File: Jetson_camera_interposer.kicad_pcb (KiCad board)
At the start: 6 copper layers, 82.1 x 75 mm, 19 parts, among them J1 QSH-060-01-L-D-A, J2 QTH-060-01-L-D-A, J21 Conn_01x01, J22 Conn_01x01, J23 Conn_01x01, J24 Conn_01x01, J25 Conn_01x01, J26 Conn_01x01, J3 Conn_01x01, J4 Conn_01x01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

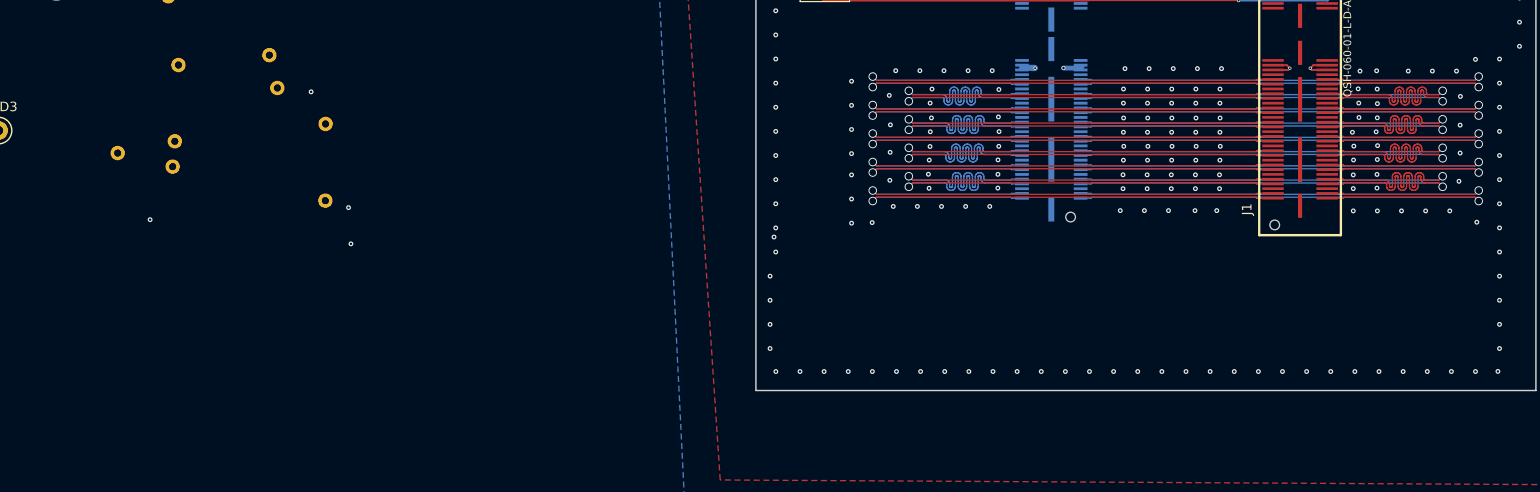
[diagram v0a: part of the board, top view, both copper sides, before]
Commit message: removed vias
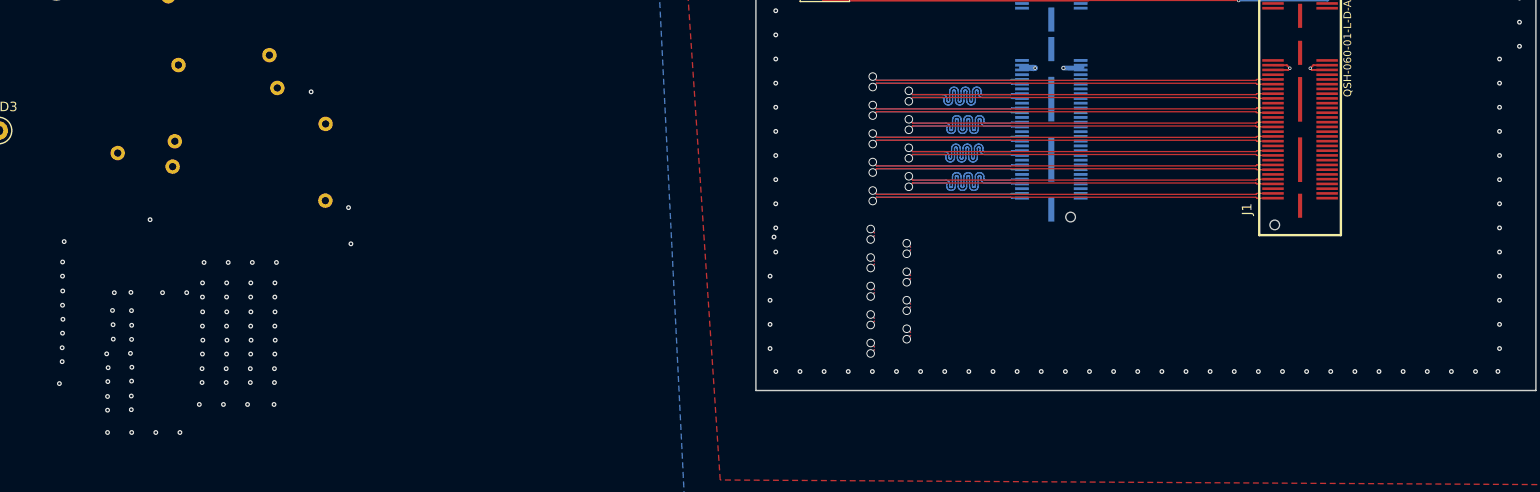
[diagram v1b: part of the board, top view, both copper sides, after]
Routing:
- net /CSI0_D1_N: track 58.3 -> 1.13 mm
- net /CSI2_CLK_P: track 58.3 -> 1.13 mm
- net /CSI4_D0_P: track 58.3 -> 1.13 mm
- net /CSI4_D0_N: track 58.3 -> 1.13 mm
- net /CSI2_CLK_N: track 58.3 -> 1.13 mm
- net /CSI0_D0_P: track 58.3 -> 1.13 mm
- net /CSI0_D0_N: track 58.3 -> 1.13 mm
- net /CSI0_D1_P: track 58.3 -> 1.13 mm
- net /CSI4_D1_N: track 58.3 -> 1.13 mm
- net /CSI4_D1_P: track 58.3 -> 1.13 mm
- net /CSI4_CLK_P: track 58.3 -> 1.13 mm
- net /CSI2_D0_P: track 58.3 -> 1.13 mm
- net /CSI2_D1_P: track 58.3 -> 1.13 mm
- net /CSI0_CLK_P: track 58.3 -> 1.13 mm
- net /CSI4_CLK_N: track 58.3 -> 1.13 mm
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
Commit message: DRC OK
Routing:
- net /CSI0_D1_N: track 1.13 -> 58.3 mm
- net /CSI2_CLK_P: track 1.13 -> 58.3 mm
- net /CSI4_D0_P: track 1.13 -> 58.3 mm
- net /CSI4_D0_N: track 1.13 -> 58.3 mm
- net /CSI2_CLK_N: track 1.13 -> 58.3 mm
- net /CSI0_D0_P: track 1.13 -> 58.3 mm
- net /CSI0_D0_N: track 1.13 -> 58.3 mm
- net /CSI0_D1_P: track 1.13 -> 58.3 mm
- net /CSI4_D1_N: track 1.13 -> 58.3 mm
- net /CSI4_D1_P: track 1.13 -> 58.3 mm
- net /CSI4_CLK_P: track 1.13 -> 58.3 mm
- net /CSI2_D0_P: track 1.13 -> 58.3 mm
- net /CSI2_D1_P: track 1.13 -> 58.3 mm
- net /CSI0_CLK_P: track 1.13 -> 58.3 mm
- net /CSI2_D0_N: track 1.13 -> 58.3 mm
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
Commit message: Done routing
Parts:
- removed GND1, GND2, GND3: TestP, TX2_Footprints:test_point
- removed J21, J22, J23, J24, J25, J4, J5, J6: Conn_01x01, TX2_Footprints:ground_probe
- added J7: Conn_01x01, Pin_Headers:Pin_Header_Straight_1x01_Pitch2.54mm, F.Cu at (4.15, 39.9)
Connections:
- J1 pad 117: (no net) -> /CAM_INTR
- J1 pad 119: (no net) -> /VSYS_EN
- J2 pad 117: (no net) -> /CAM_INTR
- J2 pad 119: (no net) -> /VSYS_EN
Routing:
- net /VSYS_EN: track 0.00 -> 27.4 mm, vias 0 -> 1
- net /CAM_INTR: track 0.00 -> 26.8 mm, vias 0 -> 2
- net /I2C_GP0_DAT_1V8_J: track 62.4 -> 66.1 mm
- net /VDD_SYS: track 32.3 -> 33.3 mm

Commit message: placed jumpers
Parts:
- removed GND4, I2C_CLK2, I2C_DAT2: TestP, TX2_Footprints:test_point
- removed J26: Conn_01x01, TX2_Footprints:ground_probe
- added J10: JETSON_1V8, Pin_Headers:Pin_Header_Straight_1x01_Pitch2.54mm, F.Cu at (112.2, 76.8)
- added J11: VDD_3V3, Pin_Headers:Pin_Header_Straight_1x01_Pitch2.54mm, F.Cu at (108.4, 84.1)
- added J12: VDD_SYS, Pin_Headers:Pin_Header_Straight_1x01_Pitch2.54mm, F.Cu at (123.3, 71.3)
- added J13: VDD_CAM_FQ_HV_CAM, Pin_Headers:Pin_Header_Straight_1x01_Pitch2.54mm, F.Cu at (130.5, 103.1)
- added J14: CAM_AF_PWDN, Pin_Headers:Pin_Header_Straight_1x01_Pitch2.54mm, F.Cu at (164.2, 101.6)
- added J15: CAM_FLASH_EN, Pin_Headers:Pin_Header_Straight_1x01_Pitch2.54mm, F.Cu at (164.2, 94.4)
- added J16: JETSON_1V2, Pin_Headers:Pin_Header_Straight_1x01_Pitch2.54mm, F.Cu at (164.2, 98.0)
- added J17: VDD_IR, Pin_Headers:Pin_Header_Straight_1x01_Pitch2.54mm, F.Cu at (160.6, 90.8)
- added J18: IR_READY, Pin_Headers:Pin_Header_Straight_1x01_Pitch2.54mm, F.Cu at (164.2, 90.8)
- added J19: CAM_INTR, Pin_Headers:Pin_Header_Straight_1x01_Pitch2.54mm, F.Cu at (164.2, 83.5)
- added J20: IR_TRIGGER, Pin_Headers:Pin_Header_Straight_1x01_Pitch2.54mm, F.Cu at (164.2, 87.2)
- added J21: VSYS_EN, Pin_Headers:Pin_Header_Straight_1x01_Pitch2.54mm, F.Cu at (164.2, 79.9)
- added J22: GND, Pin_Headers:Pin_Header_Straight_1x01_Pitch2.54mm, F.Cu at (163.0, 127.2)
- added J23: GND, Pin_Headers:Pin_Header_Straight_1x01_Pitch2.54mm, F.Cu at (96.6, 132.5)
- added J4: DVDD_CAM_LV, Pin_Headers:Pin_Header_Straight_1x01_Pitch2.54mm, F.Cu at (111.6, 104.0)
- added J5: AVDD_CAM, Pin_Headers:Pin_Header_Straight_1x01_Pitch2.54mm, F.Cu at (95.4, 104.0)
- added J6: VDD_AF, Pin_Headers:Pin_Header_Straight_1x01_Pitch2.54mm, F.Cu at (99.0, 104.0)
- added J9: CAM_VSYNC, Pin_Headers:Pin_Header_Straight_1x01_Pitch2.54mm, F.Cu at (126.9, 103.1)
- J3: value Conn_01x01 -> GND; footprint TX2_Footprints:ground_probe -> Pin_Headers:Pin_Header_Straight_1x01_Pitch2.54mm
- J7: value Conn_01x01 -> GND
- moved J7 114.9 mm to (94.0, 111.5)
- moved J3 95.4 mm to (110.7, 70.8)
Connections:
- J7 pad 1: (no net) -> Earth
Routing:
- net /CAM0_RST: track 33.6 -> 34.8 mm
- net /CAM1_RST_L_J: track 61.8 -> 62.8 mm
- net /DVDD_CAM_LV: track 47.8 -> 46.8 mm
- net /CAM0_MCLK_J: track 61.3 -> 62.1 mm

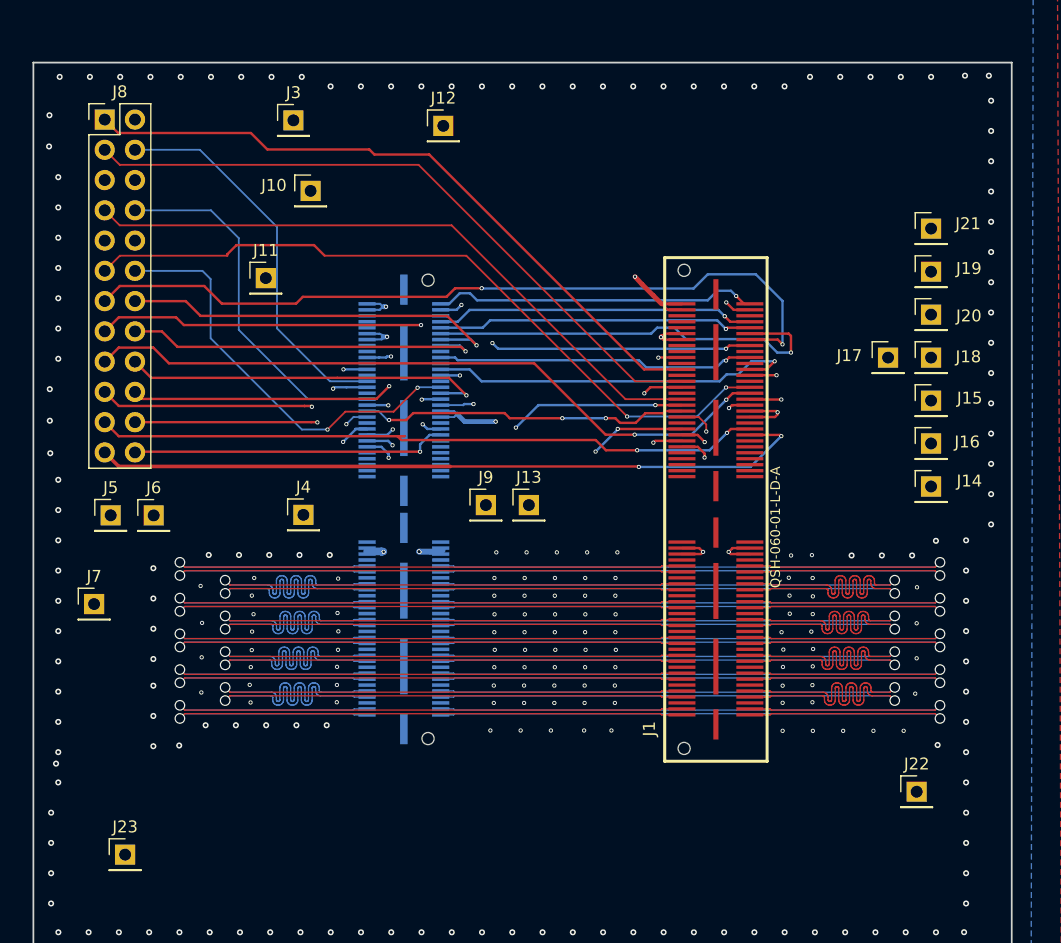
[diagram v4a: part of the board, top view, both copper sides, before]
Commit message: placed debug connectors
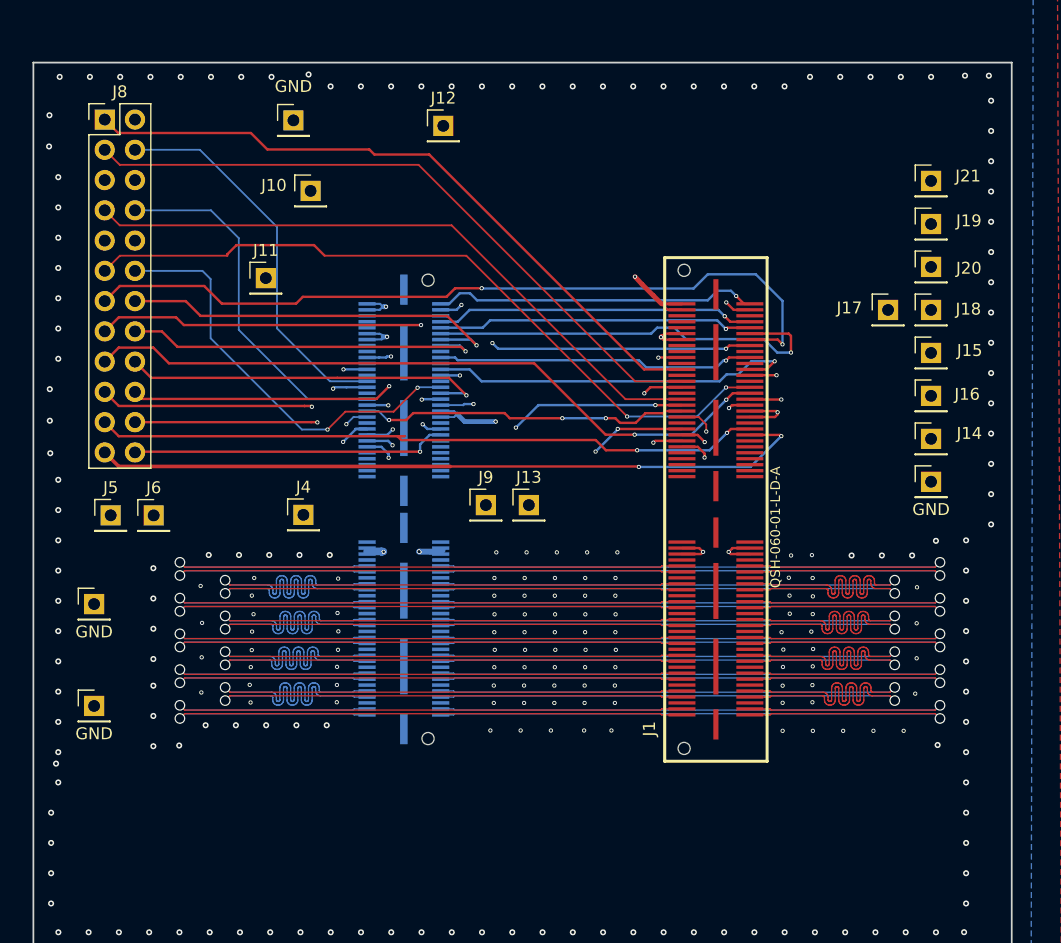
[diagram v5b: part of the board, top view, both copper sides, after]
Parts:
- moved J22 26.0 mm to (164.2, 101.2)
- moved J23 12.7 mm to (94.0, 120.0)
- moved J14 4.00 mm to (164.2, 97.6)
- moved J15 4.00 mm to (164.2, 90.4)
- moved J16 4.00 mm to (164.2, 94.0)
- moved J17 4.00 mm to (160.6, 86.8)
- moved J18 4.00 mm to (164.2, 86.8)
- moved J19 4.00 mm to (164.2, 79.5)
- moved J20 4.00 mm to (164.2, 83.2)
- moved J21 4.00 mm to (164.2, 75.9)
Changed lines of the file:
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@@
   )
   (module Pin_Headers:Pin_Header_Straight_1x01_Pitch2.54mm (layer F.Cu)
-    (at 164.25 101.58)
+    (at 164.25 97.58)
     (descr "Through hole straight pin header, 1x01, 2.54mm pitch, single row")
     (tags "Through hole pin header THT 1x01 2.54mm single row")
@@
   )
   (module Pin_Headers:Pin_Header_Straight_1x01_Pitch2.54mm (layer F.Cu)
-    (at 164.25 94.37)
+    (at 164.25 90.37)
     (descr "Through hole straight pin header, 1x01, 2.54mm pitch, single row")
     (tags "Through hole pin header THT 1x01 2.54mm single row")
@@
   )
   (module Pin_Headers:Pin_Header_Straight_1x01_Pitch2.54mm (layer F.Cu)
-    (at 164.25 97.97)
+    (at 164.25 93.97)
     (descr "Through hole straight pin header, 1x01, 2.54mm pitch, single row")
     (tags "Through hole pin header THT 1x01 2.54mm single row")
@@
   )
   (module Pin_Headers:Pin_Header_Straight_1x01_Pitch2.54mm (layer F.Cu)
-    (at 160.64 90.76)
+    (at 160.64 86.76)
     (descr "Through hole straight pin header, 1x01, 2.54mm pitch, single row")
     (tags "Through hole pin header THT 1x01 2.54mm single row")
@@
   )
   (module Pin_Headers:Pin_Header_Straight_1x01_Pitch2.54mm (layer F.Cu)
-    (at 164.25 90.76)
+    (at 164.25 86.76)
     (descr "Through hole straight pin header, 1x01, 2.54mm pitch, single row")
     (tags "Through hole pin header THT 1x01 2.54mm single row")
@@
   )
   (module Pin_Headers:Pin_Header_Straight_1x01_Pitch2.54mm (layer F.Cu)
-    (at 164.25 83.55)
+    (at 164.25 79.55)
     (descr "Through hole straight pin header, 1x01, 2.54mm pitch, single row")
     (tags "Through hole pin header THT 1x01 2.54mm single row")
@@
   )
   (module Pin_Headers:Pin_Header_Straight_1x01_Pitch2.54mm (layer F.Cu)
-    (at 164.25 87.15)
+    (at 164.25 83.15)
     (descr "Through hole straight pin header, 1x01, 2.54mm pitch, single row")
     (tags "Through hole pin header THT 1x01 2.54mm single row")
@@
   )
   (module Pin_Headers:Pin_Header_Straight_1x01_Pitch2.54mm (layer F.Cu)
-    (at 164.25 79.93)
+    (at 164.25 75.93)
     (descr "Through hole straight pin header, 1x01, 2.54mm pitch, single row")
     (tags "Through hole pin header THT 1x01 2.54mm single row")
@@
     (descr "Through hole straight pin header, 1x01, 2.54mm pitch, single row")
     (tags "Through hole pin header THT 1x01 2.54mm single row")
-    (fp_text reference J3 (at 0 -2.33) (layer F.SilkS)
-      (effects (font (size 1 1) (thickness 0.15)))
-    )
-    (fp_text value GND (at 0 2.33) (layer F.Fab)
+    (fp_text reference J3 (at 0 -2.33) (layer F.SilkS) hide
+      (effects (font (size 1 1) (thickness 0.15)))
+    )
+    (fp_text value GND (at 0 -2.85) (layer F.SilkS)
       (effects (font (size 1 1) (thickness 0.15)))
     )
@@
     (descr "Through hole straight pin header, 1x01, 2.54mm pitch, single row")
     (tags "Through hole pin header THT 1x01 2.54mm single row")
-    (fp_text reference J7 (at 0 -2.33) (layer F.SilkS)
-      (effects (font (size 1 1) (thickness 0.15)))
-    )
-    (fp_text value GND (at 0 2.33) (layer F.Fab)
+    (fp_text reference J7 (at 0 -2.33) (layer F.SilkS) hide
+      (effects (font (size 1 1) (thickness 0.15)))
+    )
+    (fp_text value GND (at 0 2.33) (layer F.SilkS)
       (effects (font (size 1 1) (thickness 0.15)))
     )
@@
   )
   (module Pin_Headers:Pin_Header_Straight_1x01_Pitch2.54mm (layer F.Cu)
-    (at 163.04 127.2)
-    (descr "Through hole straight pin header, 1x01, 2.54mm pitch, single row")
-    (tags "Through hole pin header THT 1x01 2.54mm single row")
-    (fp_text reference J22 (at 0 -2.33) (layer F.SilkS)
-      (effects (font (size 1 1) (thickness 0.15)))
-    )
-    (fp_text value GND (at 0 2.33) (layer F.Fab)
+    (at 164.25 101.18)
+    (descr "Through hole straight pin header, 1x01, 2.54mm pitch, single row")
+    (tags "Through hole pin header THT 1x01 2.54mm single row")
+    (fp_text reference J22 (at 0 -2.33) (layer F.SilkS) hide
+      (effects (font (size 1 1) (thickness 0.15)))
+    )
+    (fp_text value GND (at 0 2.33) (layer F.SilkS)
       (effects (font (size 1 1) (thickness 0.15)))
     )
@@
   )
   (module Pin_Headers:Pin_Header_Straight_1x01_Pitch2.54mm (layer F.Cu)
-    (at 96.6 132.48)
-    (descr "Through hole straight pin header, 1x01, 2.54mm pitch, single row")
-    (tags "Through hole pin header THT 1x01 2.54mm single row")
-    (fp_text reference J23 (at 0 -2.33) (layer F.SilkS)
-      (effects (font (size 1 1) (thickness 0.15)))
-    )
-    (fp_text value GND (at 0 2.33) (layer F.Fab)
+    (at 94 120)
+    (descr "Through hole straight pin header, 1x01, 2.54mm pitch, single row")
+    (tags "Through hole pin header THT 1x01 2.54mm single row")
+    (fp_text reference J23 (at 0 -2.33) (layer F.SilkS) hide
+      (effects (font (size 1 1) (thickness 0.15)))
+    )
+    (fp_text value GND (at 0 2.33) (layer F.SilkS)
       (effects (font (size 1 1) (thickness 0.15)))
     )
@@
   )
   (dimension 10.040603 (width 0.15) (layer Dwgs.User)
-    (gr_text "10.041 mm" (at 155.836812 125.660505 359.3722825) (layer Dwgs.User)
-      (effects (font (size 1 1) (thickness 0.15)))
-    )
-    (feature1 (pts (xy 160.84 127.25) (xy 160.848995 126.429042)))
-    (feature2 (pts (xy 150.8 127.14) (xy 150.808995 126.319042)))
-    (crossbar (pts (xy 150.80257 126.905427) (xy 160.84257 127.015427)))
-    (arrow1a (pts (xy 160.84257 127.015427) (xy 159.709709 127.589471)))
-    (arrow1b (pts (xy 160.84257 127.015427) (xy 159.722558 126.4167)))
-    (arrow2a (pts (xy 150.80257 126.905427) (xy 151.922582 127.504154)))
-    (arrow2b (pts (xy 150.80257 126.905427) (xy 151.935431 126.331383)))
+    (gr_text "10.041 mm" (at 156.134242 81.035078 359.3722825) (layer Dwgs.User)
+      (effects (font (size 1 1) (thickness 0.15)))
+    )
+    (feature1 (pts (xy 161.13743 82.624573) (xy 161.146425 81.803615)))
+    (feature2 (pts (xy 151.09743 82.514573) (xy 151.106425 81.693615)))
+    (crossbar (pts (xy 151.1 82.28) (xy 161.14 82.39)))
+    (arrow1a (pts (xy 161.14 82.39) (xy 160.007139 82.964044)))
+    (arrow1b (pts (xy 161.14 82.39) (xy 160.019988 81.791273)))
+    (arrow2a (pts (xy 151.1 82.28) (xy 152.220012 82.878727)))
+    (arrow2b (pts (xy 151.1 82.28) (xy 152.232861 81.705956)))
   )
   (dimension 10.340309 (width 0.15) (layer Dwgs.User)
-    (gr_text "10.340 mm" (at 136.967752 126.567019 0.4432853873) (layer Dwgs.User)
-      (effects (font (size 1 1) (thickness 0.15)))
-    )
-    (feature1 (pts (xy 131.81 128.19) (xy 131.803273 127.320577)))
-    (feature2 (pts (xy 142.15 128.11) (xy 142.143273 127.240577)))
-    (crossbar (pts (xy 142.14781 127.82698) (xy 131.80781 127.90698)))
-    (arrow1a (pts (xy 131.80781 127.90698) (xy 132.929743 127.311861)))
-    (arrow1b (pts (xy 131.80781 127.90698) (xy 132.938817 128.484668)))
-    (arrow2a (pts (xy 142.14781 127.82698) (xy 141.016803 127.249292)))
-    (arrow2b (pts (xy 142.14781 127.82698) (xy 141.025877 128.422099)))
+    (gr_text "10.340 mm" (at 136.619942 81.150039 0.4432853873) (layer Dwgs.User)
+      (effects (font (size 1 1) (thickness 0.15)))
+    )
+    (feature1 (pts (xy 131.46219 82.77302) (xy 131.455463 81.903597)))
+    (feature2 (pts (xy 141.80219 82.69302) (xy 141.795463 81.823597)))
+    (crossbar (pts (xy 141.8 82.41) (xy 131.46 82.49)))
+    (arrow1a (pts (xy 131.46 82.49) (xy 132.581933 81.894881)))
+    (arrow1b (pts (xy 131.46 82.49) (xy 132.591007 83.067688)))
+    (arrow2a (pts (xy 141.8 82.41) (xy 140.668993 81.832312)))
+    (arrow2b (pts (xy 141.8 82.41) (xy 140.678067 83.005119)))
   )
   (gr_line (start 154.97 70) (end 154.97 137) (layer Dwgs.User) (width 0.15))
@@
   (via (at 106.35 67.2) (size 0.508) (drill 0.254) (layers F.Cu B.Cu) (net 1))
   (via (at 108.89 67.2) (size 0.508) (drill 0.254) (layers F.Cu B.Cu) (net 1))
-  (via (at 111.43 67.2) (size 0.508) (drill 0.254) (layers F.Cu B.Cu) (net 1))
+  (via (at 112 67) (size 0.508) (drill 0.254) (layers F.Cu B.Cu) (net 1))
   (via (at 113.85 68) (size 0.508) (drill 0.254) (layers F.Cu B.Cu) (net 1))
   (via (at 116.39 68) (size 0.508) (drill 0.254) (layers F.Cu B.Cu) (net 1))
